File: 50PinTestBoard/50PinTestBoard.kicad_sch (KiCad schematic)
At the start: 128 parts, among them J1 Keithley_50-Pin_Connector, Q1 BC848W, Q10 BC848W, Q11 BC848W, Q12 BC848W, Q13 BC848W, Q14 BC848W, Q15 BC848W, Q18 BC848W, Q19 BC848W, Q2 BC848W, Q20 BC848W, Q21 BC848W, Q22 BC848W, Q23 BC848W, Q24 BC848W, Q25 BC848W, Q3 BC848W, Q4 BC848W, Q5 BC848W, Q6 BC848W, Q7 BC848W, Q8 BC848W, Q9 BC848W, SW1 SW_SPST, SW2 SW_SPST, SW3 SW_Push

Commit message: 50PinTestBoard: Rev 1.0
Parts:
- added TP1, TP2: TestPoint, TestPoint:TestPoint_THTPad_2.0x2.0mm_Drill1.0mm, symbol Connector:TestPoint
- TP10: renamed from TP6; footprint TestPoint:TestPoint_Pad_2.0x2.0mm -> TestPoint:TestPoint_THTPad_2.0x2.0mm_Drill1.0mm
- TP11: renamed from TP5; footprint TestPoint:TestPoint_Pad_2.0x2.0mm -> TestPoint:TestPoint_THTPad_2.0x2.0mm_Drill1.0mm
- TP12: renamed from TP4; footprint TestPoint:TestPoint_Pad_2.0x2.0mm -> TestPoint:TestPoint_THTPad_2.0x2.0mm_Drill1.0mm
- TP13: renamed from TP3; footprint TestPoint:TestPoint_Pad_2.0x2.0mm -> TestPoint:TestPoint_THTPad_2.0x2.0mm_Drill1.0mm
- TP14: renamed from TP2; footprint TestPoint:TestPoint_Pad_2.0x2.0mm -> TestPoint:TestPoint_THTPad_2.0x2.0mm_Drill1.0mm
- TP15: renamed from TP1; footprint TestPoint:TestPoint_Pad_2.0x2.0mm -> TestPoint:TestPoint_THTPad_2.0x2.0mm_Drill1.0mm
- TP23: renamed from TP15; footprint TestPoint:TestPoint_Pad_2.0x2.0mm -> TestPoint:TestPoint_THTPad_2.0x2.0mm_Drill1.0mm
- TP24: renamed from TP14; footprint TestPoint:TestPoint_Pad_2.0x2.0mm -> TestPoint:TestPoint_THTPad_2.0x2.0mm_Drill1.0mm
- TP25: renamed from TP32; footprint TestPoint:TestPoint_Pad_2.0x2.0mm -> TestPoint:TestPoint_THTPad_2.0x2.0mm_Drill1.0mm
- TP26: renamed from TP31; footprint TestPoint:TestPoint_Pad_2.0x2.0mm -> TestPoint:TestPoint_THTPad_2.0x2.0mm_Drill1.0mm
- TP27: renamed from TP30; footprint TestPoint:TestPoint_Pad_2.0x2.0mm -> TestPoint:TestPoint_THTPad_2.0x2.0mm_Drill1.0mm
- TP28: renamed from TP29; footprint TestPoint:TestPoint_Pad_2.0x2.0mm -> TestPoint:TestPoint_THTPad_2.0x2.0mm_Drill1.0mm
- TP29: renamed from TP28; footprint TestPoint:TestPoint_Pad_2.0x2.0mm -> TestPoint:TestPoint_THTPad_2.0x2.0mm_Drill1.0mm
- TP3: renamed from TP13; footprint TestPoint:TestPoint_Pad_2.0x2.0mm -> TestPoint:TestPoint_THTPad_2.0x2.0mm_Drill1.0mm
- TP30: renamed from TP27; footprint TestPoint:TestPoint_Pad_2.0x2.0mm -> TestPoint:TestPoint_THTPad_2.0x2.0mm_Drill1.0mm
- TP31: renamed from TP26; footprint TestPoint:TestPoint_Pad_2.0x2.0mm -> TestPoint:TestPoint_THTPad_2.0x2.0mm_Drill1.0mm
- TP32: renamed from TP25; footprint TestPoint:TestPoint_Pad_2.0x2.0mm -> TestPoint:TestPoint_THTPad_2.0x2.0mm_Drill1.0mm
- TP4: renamed from TP12; footprint TestPoint:TestPoint_Pad_2.0x2.0mm -> TestPoint:TestPoint_THTPad_2.0x2.0mm_Drill1.0mm
- TP5: renamed from TP11; footprint TestPoint:TestPoint_Pad_2.0x2.0mm -> TestPoint:TestPoint_THTPad_2.0x2.0mm_Drill1.0mm
- TP6: renamed from TP10; footprint TestPoint:TestPoint_Pad_2.0x2.0mm -> TestPoint:TestPoint_THTPad_2.0x2.0mm_Drill1.0mm
- TP7: renamed from TP9; footprint TestPoint:TestPoint_Pad_2.0x2.0mm -> TestPoint:TestPoint_THTPad_2.0x2.0mm_Drill1.0mm
- TP8: footprint TestPoint:TestPoint_Pad_2.0x2.0mm -> TestPoint:TestPoint_THTPad_2.0x2.0mm_Drill1.0mm
- TP9: renamed from TP7; footprint TestPoint:TestPoint_Pad_2.0x2.0mm -> TestPoint:TestPoint_THTPad_2.0x2.0mm_Drill1.0mm
- renumbered D13 to D1, D4 to D10, D3 to D11, D2 to D12, D1 to D13, D15 to D14, D14 to D15, D18 to D16, D19 to D17, D20 to D18, D21 to D19, D12 to D2, D22 to D20, D23 to D21, D24 to D22, D25 to D23, D11 to D3, D10 to D4, D9 to D5, D8 to D6, D6 to D8, D5 to D9, Q13 to Q1, Q4 to Q10, Q3 to Q11, Q2 to Q12, Q1 to Q13, Q15 to Q14, Q14 to Q15, Q18 to Q16, Q19 to Q17, Q20 to Q18, Q21 to Q19, Q12 to Q2, Q22 to Q20, Q23 to Q21, Q24 to Q22, Q25 to Q23, Q11 to Q3, Q10 to Q4, Q9 to Q5, Q8 to Q6, Q6 to Q8, Q5 to Q9, R25 to R1, R16 to R10, R15 to R11, R14 to R12, R28 to R14, R12 to R15, R11 to R16, R10 to R17, R9 to R18, R8 to R19, R24 to R2, R7 to R20, R6 to R21, R5 to R22, R4 to R23, R3 to R24, R2 to R25, R1 to R26, R26 to R28, R33 to R29, R23 to R3, R34 to R30, R35 to R31, R36 to R32, R37 to R33, R38 to R34, R39 to R35, R40 to R36, R30 to R37, R29 to R38, R43 to R39, R22 to R4, R44 to R40, R45 to R41, R46 to R42, R47 to R43, R48 to R44, R49 to R45, R50 to R46, R21 to R5, R20 to R6, R19 to R7, R18 to R8, R17 to R9, SW3 to SW1, SW1 to SW2, SW2 to SW3, TP18 to TP16, TP21 to TP17, TP17 to TP18, TP16 to TP19, TP19 to TP21, TP24 to TP22, TP22 to TP33, TP23 to TP34
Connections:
- net +5V: now also TP2.1
- net GND: now also TP1.1
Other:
- company: (none) -> Peter Farley
- title: (none) -> Keithley 615 50-Pin Test Board

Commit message: 50PinTestBoard: Rev 1.1
Made screw holes for connector foot print plated through-holes.
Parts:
- added R47, R48: 0, Resistor_SMD:R_0603_1608Metric, symbol Device:R_Small
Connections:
- net GND: now also R47.2, R48.2
- new net: J1.51 (SHIELD), R47.1
- new net: J1.52 (SHIELD), R48.1
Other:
- moved on the sheet: TP16, TP18, TP19

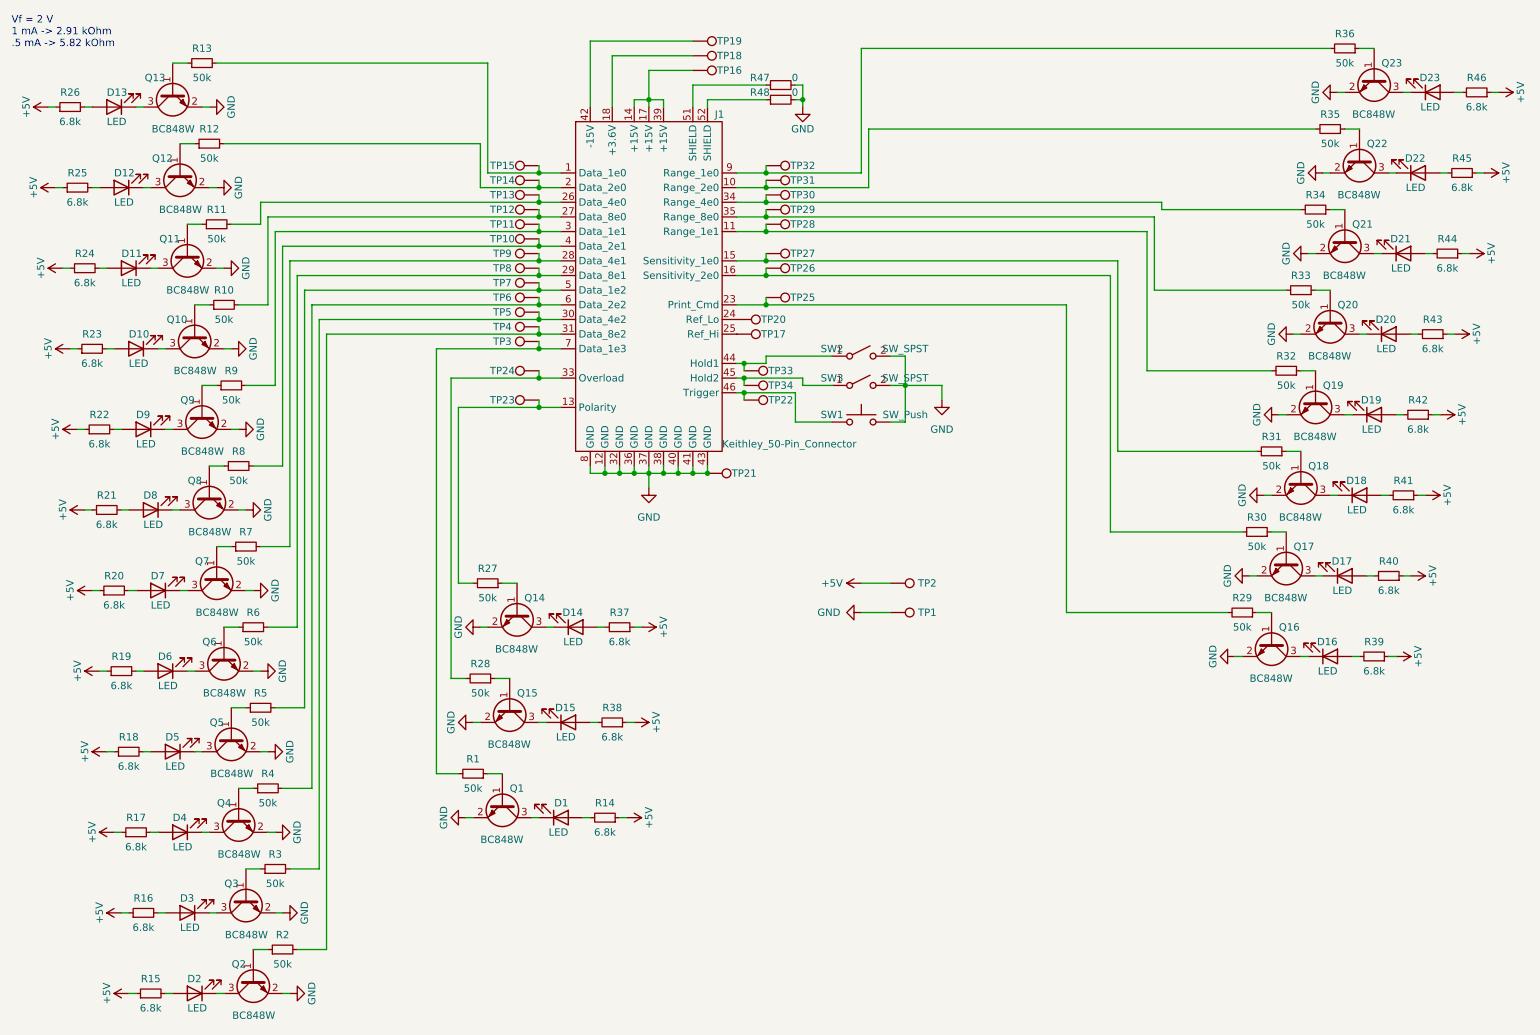
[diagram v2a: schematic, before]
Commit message: 50PinTestBoard: Rev 1.2
Fix orientation of connector footprint
 - Moved connector to bottom of board to avoid re-routing entire board.
Update resistor value(s).
Add Digi-Key links for parts.
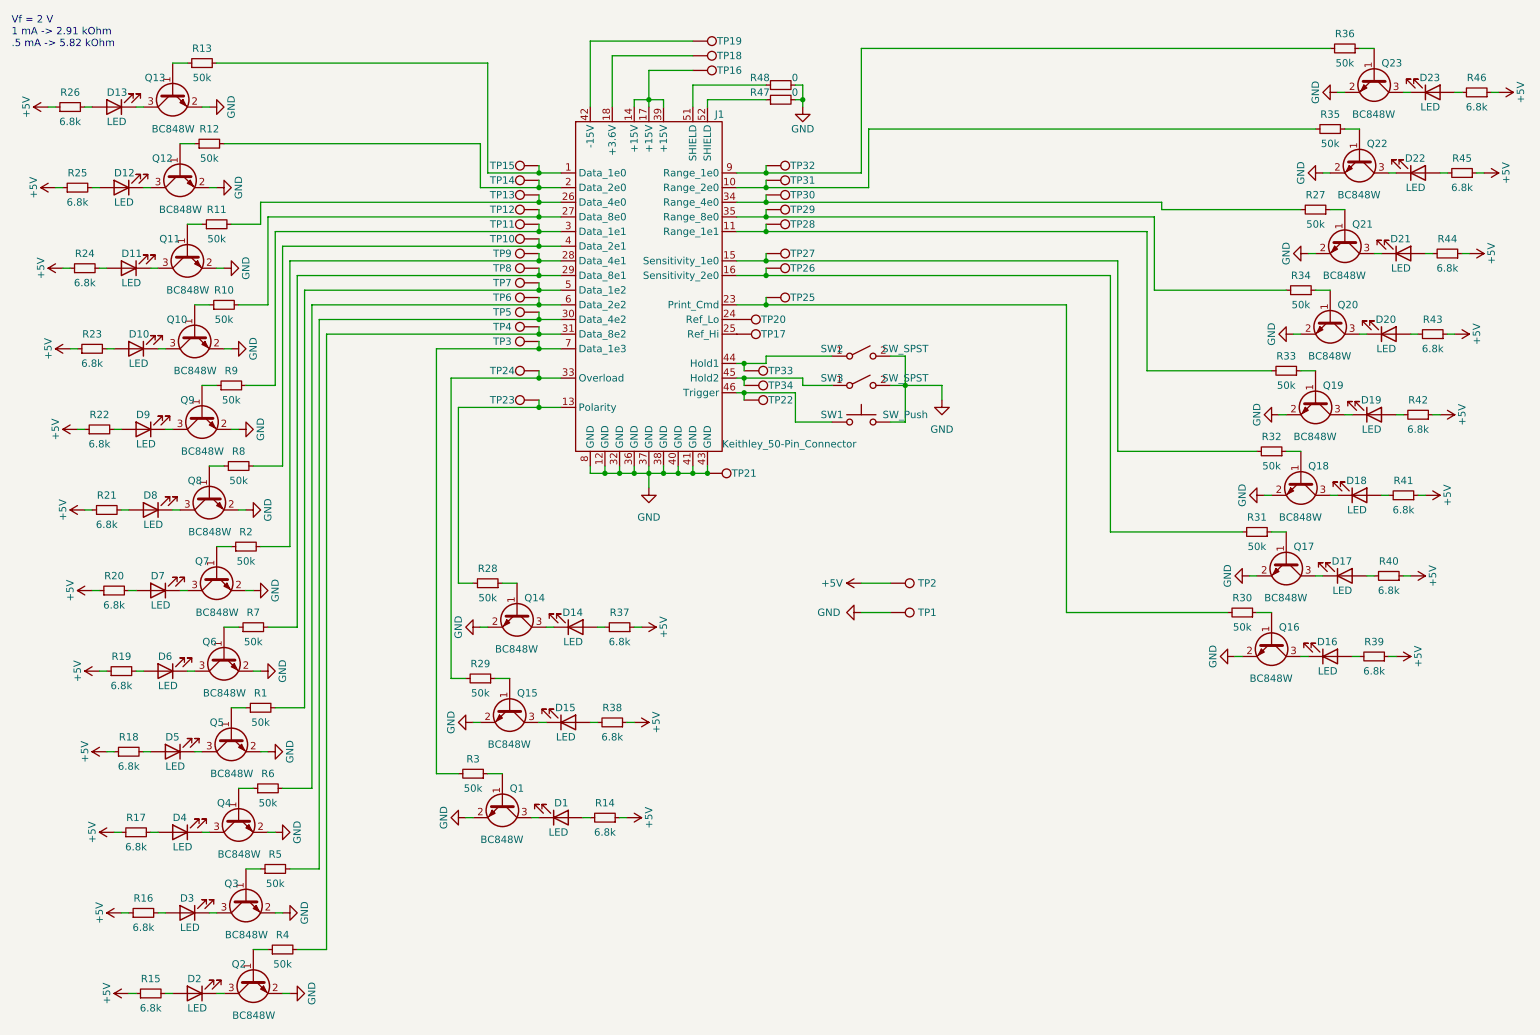
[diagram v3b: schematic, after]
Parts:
- D1, D10, D11, D12, D13, D14, D15, D16, D17, D18, D19, D2, D20, D21, D22, D23, D3, D4, D5, D6, D7, D8, D9: DigiKey (none) -> https://www.digikey.com/en/products/detail/harvatek-corpora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
- J1: DigiKey (none) -> https://www.digikey.com/en/products/detail/norcomp-inc/112-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
- Q1, Q10, Q11, Q12, Q13, Q14, Q15, Q16, Q17, Q18, Q19, Q2, Q20, Q21, Q22, Q23, Q3, Q4, Q5, Q6, Q7, Q8, Q9: DigiKey (none) -> https://www.digikey.com/en/products/detail/nexperia-usa-inc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
- R1: renamed from R5; DigiKey (none) -> https://www.digikey.com/en/products/detail/walsin-technolog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
- R10, R11, R12, R13, R14, R15, R16, R17, R18, R19, R20, R21, R22, R23, R24, R25, R26, R35, R36, R37, R38, R39, R40, R41, R42, R43, R44, R45, R46, R8, R9: DigiKey (none) -> https://www.digikey.com/en/products/detail/walsin-technolog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
- R2: renamed from R7; DigiKey (none) -> https://www.digikey.com/en/products/detail/walsin-technolog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
- R27: renamed from R34; DigiKey (none) -> https://www.digikey.com/en/products/detail/walsin-technolog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
- R28: renamed from R27; DigiKey (none) -> https://www.digikey.com/en/products/detail/walsin-technolog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
- R29: renamed from R28; DigiKey (none) -> https://www.digikey.com/en/products/detail/walsin-technolog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
- R3: renamed from R1; DigiKey (none) -> https://www.digikey.com/en/products/detail/walsin-technolog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
- R30: renamed from R29; DigiKey (none) -> https://www.digikey.com/en/products/detail/walsin-technolog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
- R31: renamed from R30; DigiKey (none) -> https://www.digikey.com/en/products/detail/walsin-technolog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
- R32: renamed from R31; DigiKey (none) -> https://www.digikey.com/en/products/detail/walsin-technolog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
- R33: renamed from R32; DigiKey (none) -> https://www.digikey.com/en/products/detail/walsin-technolog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
- R34: renamed from R33; DigiKey (none) -> https://www.digikey.com/en/products/detail/walsin-technolog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
- R4: renamed from R2; DigiKey (none) -> https://www.digikey.com/en/products/detail/walsin-technolog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
- R47: renamed from R48; DigiKey (none) -> https://www.digikey.com/en/products/detail/walsin-technolog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
- R48: renamed from R47; DigiKey (none) -> https://www.digikey.com/en/products/detail/walsin-technolog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
- R5: renamed from R3; DigiKey (none) -> https://www.digikey.com/en/products/detail/walsin-technolog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
- R6: renamed from R4; DigiKey (none) -> https://www.digikey.com/en/products/detail/walsin-technolog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
- R7: renamed from R6; DigiKey (none) -> https://www.digikey.com/en/products/detail/walsin-technolog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
- SW1: DigiKey (none) -> https://www.digikey.com/en/products/detail/c-k/PTS810-SJK-2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
- SW2, SW3: DigiKey (none) -> https://www.digikey.com/en/products/detail/c-k/JS102011SAQN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
